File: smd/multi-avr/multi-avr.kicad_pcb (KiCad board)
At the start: 2 copper layers, 57 x 56 mm, 38 parts, among them J1 USB_B_Mini, SW1 SW_SPST, U1 ATmega32U4-AU, U2 ZIF, Y1 16MHz, Y2 16MHz

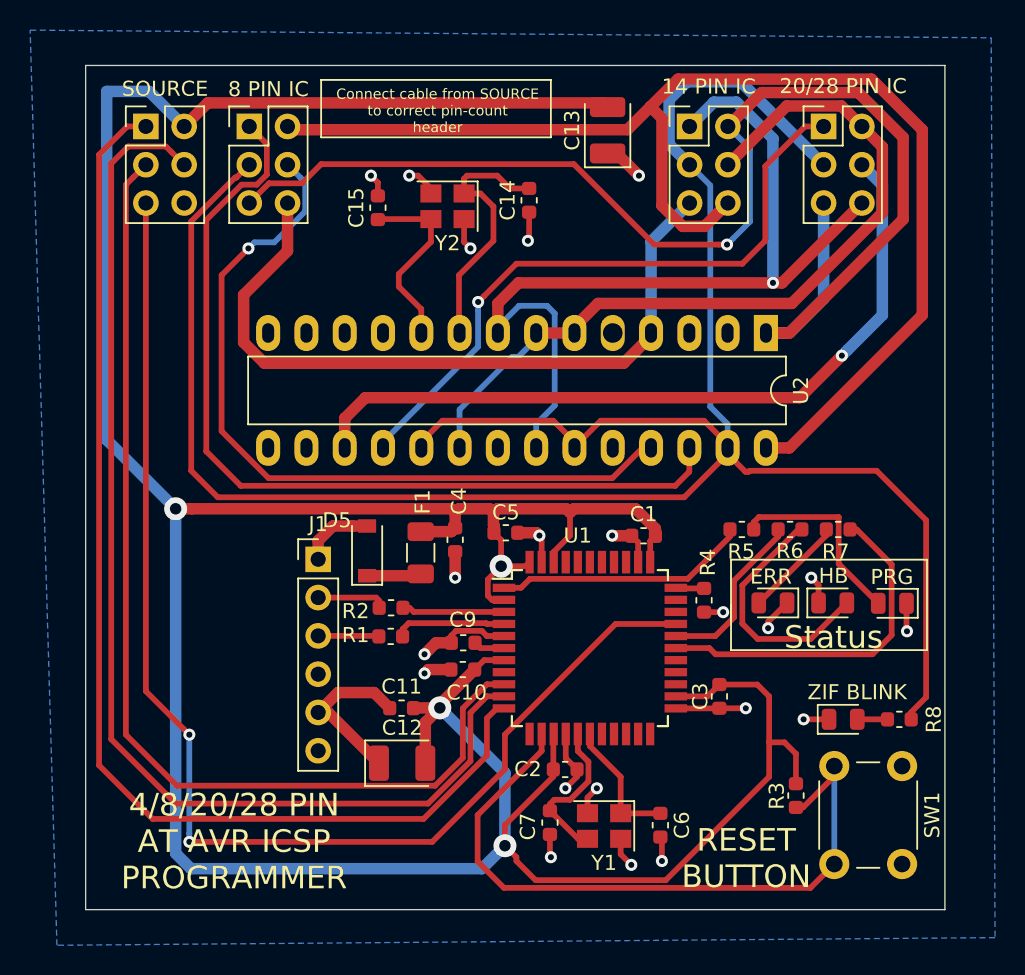
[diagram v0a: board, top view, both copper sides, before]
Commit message: Reworked schematic for the USB6 and correct caps
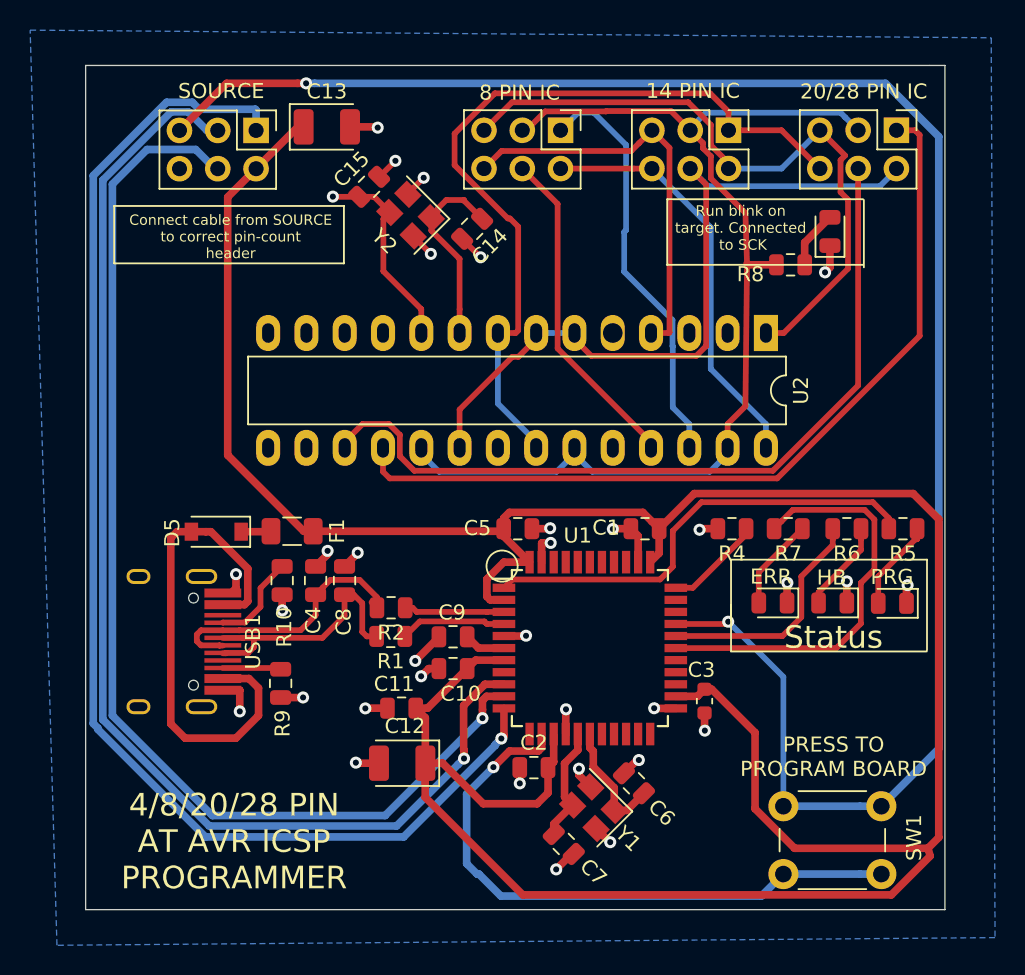
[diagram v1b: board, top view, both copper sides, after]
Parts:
- removed J1: USB_B_Mini, Connector_PinHeader_2.54mm:PinHeader_1x06_P2.54mm_Vertical
- removed R3: 10K, Resistor_SMD:R_0603_1608Metric
- added C8: 4.7uF, Capacitor_SMD:C_0805_2012Metric, F.Cu at (144.6, 98.4)
- added R10: 5.1K, Resistor_SMD:R_0805_2012Metric, F.Cu at (140.5, 98.4)
- added R9: 5.1K, Resistor_SMD:R_0805_2012Metric, F.Cu at (140.4, 105.2)
- added USB1: CLEAN-TYPE-C-31-M-12, Type-C:HRO-TYPE-C-31-M-12-HandSoldering, F.Cu at (128.3, 102.4)
- C1, C10, C11, C14, C15, C2, C4, C5, C6, C7, C9: footprint Capacitor_SMD:C_0603_1608Metric -> Capacitor_SMD:C_0805_2012Metric
- D4: value ZIF BLINK -> SCK BLINK
- R1, R2, R4, R5, R6, R7, R8: footprint Resistor_SMD:R_0603_1608Metric -> Resistor_SMD:R_0805_2012Metric
- SW1: value SW_SPST -> PRG
- moved D4 32.4 mm to (176.8, 75.2), turned to 90 degrees
- moved R8 31.0 mm to (174.2, 77.4), turned to 180 degrees
- moved CONN3 20.7 mm to (158.9, 68.5), turned to 270 degrees
- moved C13 18.6 mm to (143.4, 68.3), turned to 0 degrees
- moved R5 10.7 mm to (181.6, 94.9)
- moved D5 10.1 mm to (136.1, 95.1), turned to 180 degrees
- moved C4 9.64 mm to (142.7, 98.4), turned to 270 degrees
- moved F1 8.65 mm to (141.1, 95.1), turned to 180 degrees
- moved SW1 8.31 mm to (173.7, 113.3), turned to 0 degrees
- moved CONN1 7.31 mm to (138.7, 68.5), turned to 270 degrees
- moved R4 5.10 mm to (170.3, 94.9), turned to 180 degrees
- moved CONN2 4.84 mm to (181.2, 68.5), turned to 270 degrees
- moved C14 4.23 mm to (153.1, 75.0), turned to 225 degrees
- moved R6 3.77 mm to (177.9, 94.9)
- moved R7 3.32 mm to (174.0, 94.9), turned to 180 degrees
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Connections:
- net Net-(C6-Pad1) renamed /X+
- net Net-(C7-Pad1) renamed /X-
- C12 pad 1: GND -> +5V
- C12 pad 2: +5V -> GND
- C13 pad 1: GND -> +5V
- C13 pad 2: +5V -> GND
- C4 pad 2: +5V -> Net-(C4-Pad2)
- D5 pad 2: Net-(D5-Pad2) -> /USB_+5
- R1 pad 2: /D+ -> Net-(C8-Pad2)
- R2 pad 2: /D- -> Net-(C4-Pad2)
- R4 pad 1: GND -> Net-(R4-Pad1)
- R4 pad 2: Net-(R4-Pad2) -> GND
- SW1 pad 1: GND -> /~S_RESET
- U1 pad 33: Net-(R4-Pad2) -> Net-(R4-Pad1)
- U1 pad 42: +5V -> Net-(U1-Pad42)
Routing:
- net /SC14: track 150.2 -> 73.1 mm
- net /G14: track 84.1 -> 27.7 mm
- net /V14: track 86.6 -> 44.4 mm, vias 1 -> 0
- net /~S_RESET: track 83.2 -> 122.9 mm
- net /USB_+5: track 0.00 -> 33.8 mm
- net +5V: track 231.0 -> 198.6 mm, vias 4 -> 0
- net /MI8: track 59.3 -> 27.7 mm
- net /MO8: track 51.8 -> 22.3 mm, vias 1 -> 0
- net /G8: track 48.7 -> 27.3 mm
- net Net-(C4-Pad2): track 0.00 -> 18.2 mm
- net Net-(C8-Pad2): track 0.00 -> 17.3 mm
- net /PRG_LED: track 16.9 -> 30.4 mm
- net /MI20: track 42.9 -> 56.3 mm, vias 1 -> 0
- net GND: track 62.9 -> 51.1 mm, vias 21 -> 32
- net /S_SCK: track 69.6 -> 81.3 mm, vias 0 -> 1
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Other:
- board text added: "PRESS TO PROGRAM BOARD"
- board text added: "Run blink on target. Connected to SCK"
- board text removed: "RESET BUTTON"
